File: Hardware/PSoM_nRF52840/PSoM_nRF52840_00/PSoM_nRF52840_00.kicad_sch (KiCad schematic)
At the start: 0 parts

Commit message: working on nrf52840
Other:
- sheet nRF52840 renamed 400-nRF52840
- sheet 100_Connectors ports: added CC1, CC2, RST, SWDCLK, SWDIO; removed EN, RX0, TX0
- sheet 200_1S_Charger ports: added 3V3_EXT, 3V3_nRF, CC1, CC2, VBUS_OUT; removed none
- sheet 400-nRF52840 ports: added D+, D-, GND, IO[0..42], SPI[0..7], SWDCLK, SWDIO, VBUS, VDD_nRF; removed none

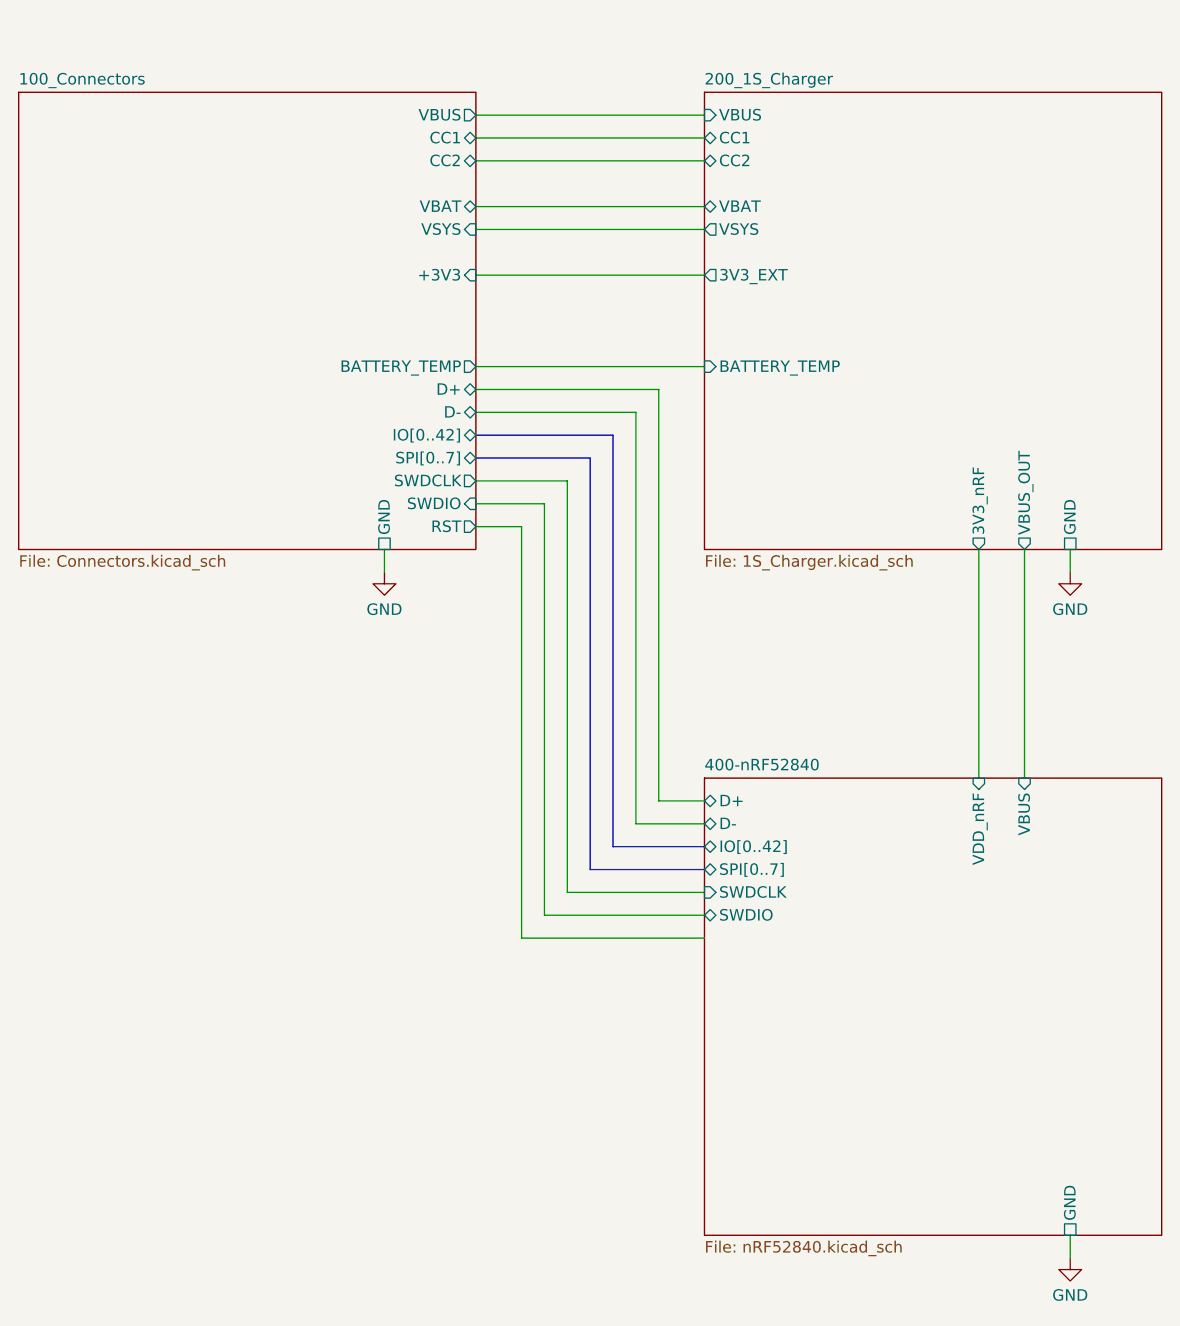
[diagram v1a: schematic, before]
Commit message: footprint assignement done
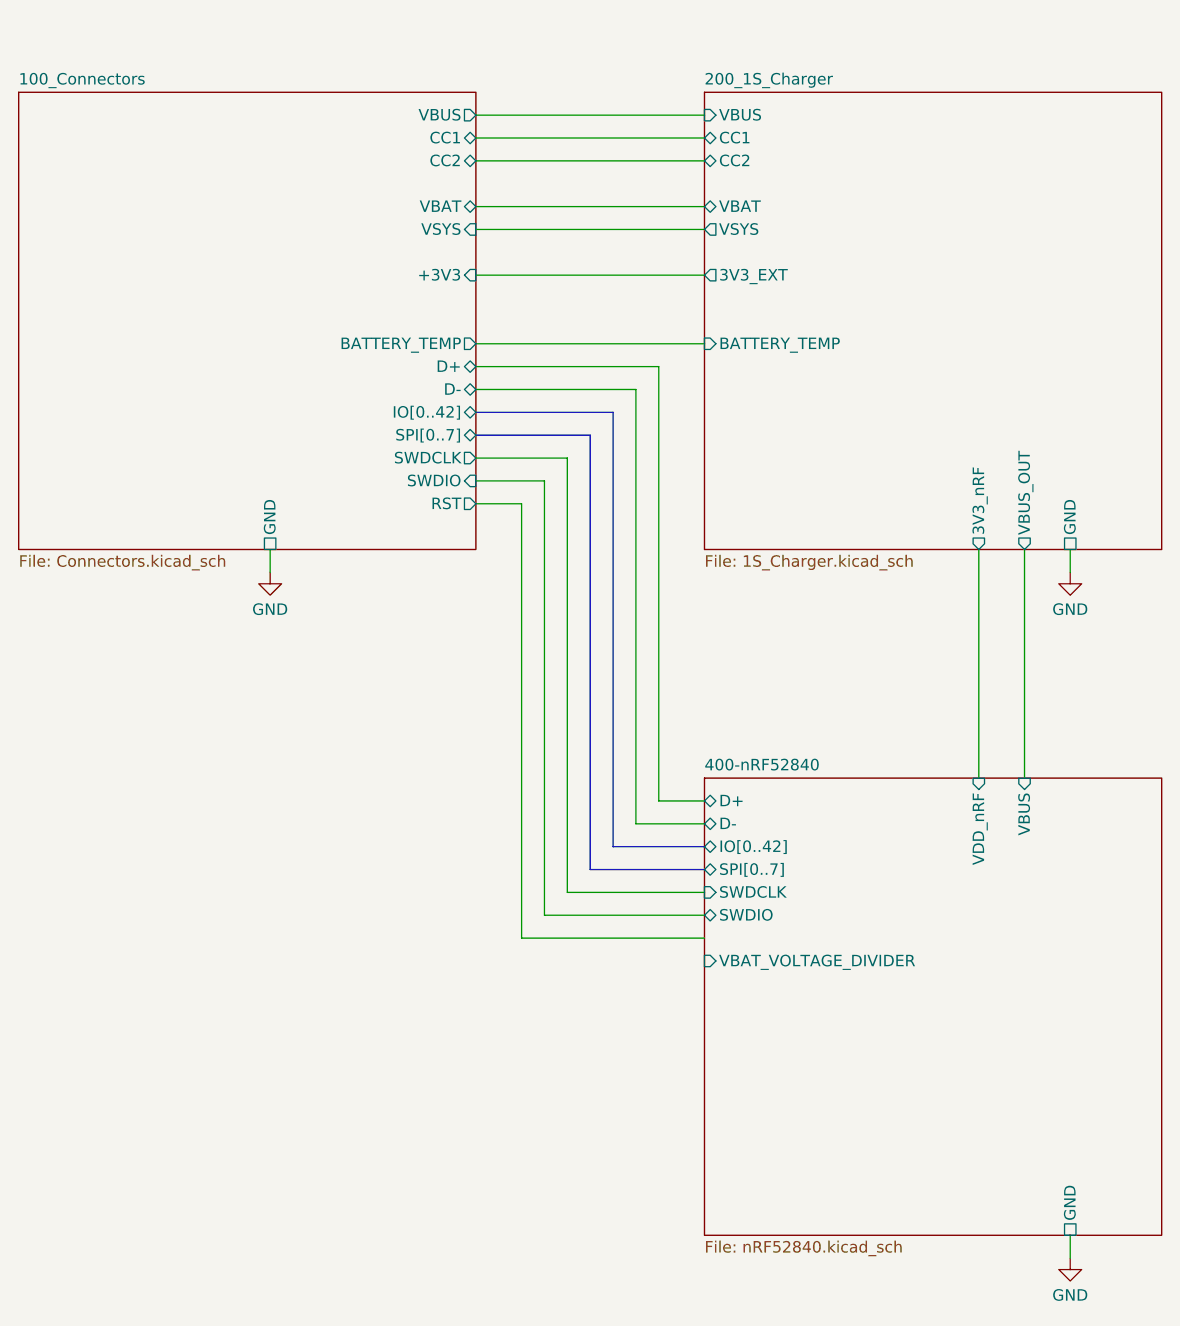
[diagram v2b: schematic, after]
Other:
- sheet 400-nRF52840 ports: added VBAT_VOLTAGE_DIVIDER; removed none
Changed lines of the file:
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@@
 	(wire
 		(pts
-			(xy 109.22 71.12) (xy 109.22 116.84)
+			(xy 109.22 68.58) (xy 109.22 116.84)
 		)
 		(stroke
@@
 	(wire
 		(pts
-			(xy 101.6 73.66) (xy 106.68 73.66)
-		)
-		(stroke
-			(width 0)
-			(type default)
-		)
-	)
-	(wire
-		(pts
-			(xy 91.44 76.2) (xy 91.44 78.74)
-		)
-		(stroke
-			(width 0)
-			(type default)
-		)
-	)
-	(wire
-		(pts
-			(xy 121.92 58.42) (xy 101.6 58.42)
-		)
-		(stroke
-			(width 0)
-			(type default)
-		)
-	)
-	(wire
-		(pts
-			(xy 106.68 73.66) (xy 106.68 119.38)
+			(xy 101.6 71.12) (xy 106.68 71.12)
+		)
+		(stroke
+			(width 0)
+			(type default)
+		)
+	)
+	(wire
+		(pts
+			(xy 78.74 76.2) (xy 78.74 78.74)
+		)
+		(stroke
+			(width 0)
+			(type default)
+		)
+	)
+	(wire
+		(pts
+			(xy 121.92 55.88) (xy 101.6 55.88)
+		)
+		(stroke
+			(width 0)
+			(type default)
+		)
+	)
+	(wire
+		(pts
+			(xy 106.68 71.12) (xy 106.68 119.38)
 		)
 		(stroke
@@
 	(wire
 		(pts
-			(xy 121.92 58.42) (xy 121.92 104.14)
+			(xy 121.92 55.88) (xy 121.92 104.14)
 		)
 		(stroke
@@
 	(wire
 		(pts
-			(xy 111.76 114.3) (xy 111.76 68.58)
+			(xy 111.76 114.3) (xy 111.76 66.04)
 		)
 		(stroke
@@
 	(bus
 		(pts
-			(xy 116.84 109.22) (xy 116.84 63.5)
+			(xy 116.84 109.22) (xy 116.84 60.96)
 		)
 		(stroke
@@
 	(wire
 		(pts
-			(xy 111.76 68.58) (xy 101.6 68.58)
+			(xy 111.76 66.04) (xy 101.6 66.04)
 		)
 		(stroke
@@
 	(bus
 		(pts
-			(xy 114.3 66.04) (xy 114.3 111.76)
+			(xy 114.3 63.5) (xy 114.3 111.76)
 		)
 		(stroke
@@
 	(wire
 		(pts
-			(xy 101.6 71.12) (xy 109.22 71.12)
-		)
-		(stroke
-			(width 0)
-			(type default)
-		)
-	)
-	(wire
-		(pts
-			(xy 119.38 60.96) (xy 119.38 106.68)
+			(xy 101.6 68.58) (xy 109.22 68.58)
+		)
+		(stroke
+			(width 0)
+			(type default)
+		)
+	)
+	(wire
+		(pts
+			(xy 119.38 58.42) (xy 119.38 106.68)
 		)
 		(stroke
@@
 	(bus
 		(pts
-			(xy 101.6 66.04) (xy 114.3 66.04)
-		)
-		(stroke
-			(width 0)
-			(type default)
-		)
-	)
-	(wire
-		(pts
-			(xy 101.6 60.96) (xy 119.38 60.96)
+			(xy 101.6 63.5) (xy 114.3 63.5)
+		)
+		(stroke
+			(width 0)
+			(type default)
+		)
+	)
+	(wire
+		(pts
+			(xy 101.6 58.42) (xy 119.38 58.42)
 		)
 		(stroke
@@
 	(bus
 		(pts
-			(xy 116.84 63.5) (xy 101.6 63.5)
-		)
-		(stroke
-			(width 0)
-			(type default)
-		)
-	)
-	(wire
-		(pts
-			(xy 101.6 55.88) (xy 127 55.88)
+			(xy 116.84 60.96) (xy 101.6 60.96)
+		)
+		(stroke
+			(width 0)
+			(type default)
+		)
+	)
+	(wire
+		(pts
+			(xy 101.6 53.34) (xy 127 53.34)
 		)
 		(stroke
@@
 	(symbol
 		(lib_id "power:GND")
-		(at 91.44 78.74 0)
+		(at 78.74 78.74 0)
 		(unit 1)
 		(exclude_from_sim no)
@@
 		(fields_autoplaced yes)
 		(property "Reference" "#PWR06"
-			(at 91.44 85.09 0)
+			(at 78.74 85.09 0)
 			(effects
 				(font
@@
 		)
 		(property "Value" "GND"
-			(at 91.44 82.8755 0)
+			(at 78.74 82.8755 0)
 			(effects
 				(font
@@
 		)
 		(property "Footprint" ""
-			(at 91.44 78.74 0)
+			(at 78.74 78.74 0)
 			(effects
 				(font
@@
 		)
 		(property "Datasheet" ""
-			(at 91.44 78.74 0)
+			(at 78.74 78.74 0)
 			(effects
 				(font
@@
 		)
 		(property "Description" ""
-			(at 91.44 78.74 0)
+			(at 78.74 78.74 0)
 			(effects
 				(font
@@
 		)
 		(pin "BATTERY_TEMP" input
-			(at 127 55.88 180)
+			(at 127 53.34 180)
 			(effects
 				(font
@@
 		)
 		(pin "D-" bidirectional
-			(at 101.6 60.96 0)
+			(at 101.6 58.42 0)
 			(effects
 				(font
@@
 		)
 		(pin "D+" bidirectional
-			(at 101.6 58.42 0)
+			(at 101.6 55.88 0)
 			(effects
 				(font
@@
 		)
 		(pin "GND" passive
-			(at 91.44 76.2 270)
+			(at 78.74 76.2 270)
 			(effects
 				(font
@@
 		)
 		(pin "IO[0..42]" bidirectional
-			(at 101.6 63.5 0)
+			(at 101.6 60.96 0)
 			(effects
 				(font
@@
 		)
 		(pin "SPI[0..7]" bidirectional
-			(at 101.6 66.04 0)
+			(at 101.6 63.5 0)
 			(effects
 				(font
@@
 		)
 		(pin "BATTERY_TEMP" output
-			(at 101.6 55.88 0)
+			(at 101.6 53.34 0)
 			(effects
 				(font
@@
 		)
 		(pin "SWDCLK" output
+			(at 101.6 66.04 0)
+			(effects
+				(font
+					(size 1.27 1.27)
+				)
+				(justify right)
+			)
+		)
+		(pin "SWDIO" input
 			(at 101.6 68.58 0)
-			(effects
-				(font
-					(size 1.27 1.27)
-				)
-				(justify right)
-			)
-		)
-		(pin "SWDIO" input
-			(at 101.6 71.12 0)
 			(effects
 				(font
@@
 		)
 		(pin "RST" output
-			(at 101.6 73.66 0)
+			(at 101.6 71.12 0)
 			(effects
 				(font
@@
 			)
 		)
+		(pin "VBAT_VOLTAGE_DIVIDER" input
+			(at 127 121.92 180)
+			(effects
+				(font
+					(size 1.27 1.27)
+				)
+				(justify left)
+			)
+		)

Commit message: working on schematic
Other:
- sheet 100_Connectors ports: added P[0..52]; removed IO[0..42]
- sheet 400-nRF52840 ports: added P[0..52], RESET; removed IO[0..42], VBAT_VOLTAGE_DIVIDER
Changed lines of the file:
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@@
 	(wire
 		(pts
-			(xy 78.74 76.2) (xy 78.74 78.74)
+			(xy 76.2 76.2) (xy 76.2 78.74)
 		)
 		(stroke
@@
 	(symbol
 		(lib_id "power:GND")
-		(at 78.74 78.74 0)
+		(at 76.2 78.74 0)
 		(unit 1)
 		(exclude_from_sim no)
@@
 		(fields_autoplaced yes)
 		(property "Reference" "#PWR06"
-			(at 78.74 85.09 0)
+			(at 76.2 85.09 0)
 			(effects
 				(font
@@
 		)
 		(property "Value" "GND"
-			(at 78.74 82.8755 0)
+			(at 76.2 82.8755 0)
 			(effects
 				(font
@@
 		)
 		(property "Footprint" ""
-			(at 78.74 78.74 0)
+			(at 76.2 78.74 0)
 			(effects
 				(font
@@
 		)
 		(property "Datasheet" ""
-			(at 78.74 78.74 0)
+			(at 76.2 78.74 0)
 			(effects
 				(font
@@
 		)
 		(property "Description" ""
-			(at 78.74 78.74 0)
+			(at 76.2 78.74 0)
 			(effects
 				(font
@@
 		)
 		(pin "GND" passive
-			(at 78.74 76.2 270)
-			(effects
-				(font
-					(size 1.27 1.27)
-				)
-				(justify left)
-			)
-		)
-		(pin "IO[0..42]" bidirectional
-			(at 101.6 60.96 0)
-			(effects
-				(font
-					(size 1.27 1.27)
-				)
-				(justify right)
+			(at 76.2 76.2 270)
+			(effects
+				(font
+					(size 1.27 1.27)
+				)
+				(justify left)
 			)
 		)
@@
 		(pin "RST" output
 			(at 101.6 71.12 0)
+			(effects
+				(font
+					(size 1.27 1.27)
+				)
+				(justify right)
+			)
+		)
+		(pin "P[0..52]" bidirectional
+			(at 101.6 60.96 0)
 			(effects
 				(font
@@
 			)
 		)
-		(pin "IO[0..42]" bidirectional
-			(at 127 109.22 180)
-			(effects
-				(font
-					(size 1.27 1.27)
-				)
-				(justify left)
-			)
-		)
 		(pin "VBUS" input
 			(at 162.56 101.6 90)
@@
 			)
 		)
-		(pin "VBAT_VOLTAGE_DIVIDER" input
-			(at 127 121.92 180)
-			(effects
-				(font
+		(pin "RESET" input
+			(at 127 119.38 180)
+			(effects
+				(font
+					(size 1.27 1.27)
+				)
+				(justify left)
+			)
+		)
+		(pin "P[0..52]" bidirectional
+			(at 127 109.22 180)
+			(effects
+				(font

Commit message: schematic should be done
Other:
- sheet 200_1S_Charger ports: added SCL, SDA; removed none
- sheet 400-nRF52840 ports: added SCL, SDA; removed none
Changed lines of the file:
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@@
+	(wire
+		(pts
+			(xy 167.64 101.6) (xy 167.64 76.2)
+		)
+		(stroke
+			(width 0)
+			(type default)
+		)
+	)
 	(wire
 		(pts
@@
 	(wire
 		(pts
-			(xy 162.56 76.2) (xy 162.56 101.6)
+			(xy 160.02 76.2) (xy 160.02 101.6)
 		)
 		(stroke
@@
 	(wire
 		(pts
+			(xy 165.1 76.2) (xy 165.1 101.6)
+		)
+		(stroke
+			(width 0)
+			(type default)
+		)
+	)
+	(wire
+		(pts
 			(xy 111.76 66.04) (xy 101.6 66.04)
 		)
@@
 	(wire
 		(pts
-			(xy 167.64 76.2) (xy 167.64 78.74)
+			(xy 175.26 76.2) (xy 175.26 78.74)
 		)
 		(stroke
@@
 	(symbol
 		(lib_id "power:GND")
-		(at 167.64 78.74 0)
+		(at 175.26 78.74 0)
 		(unit 1)
 		(exclude_from_sim no)
@@
 		(fields_autoplaced yes)
 		(property "Reference" "#PWR07"
-			(at 167.64 85.09 0)
+			(at 175.26 85.09 0)
 			(effects
 				(font
@@
 		)
 		(property "Value" "GND"
-			(at 167.64 82.8755 0)
+			(at 175.26 82.8755 0)
 			(effects
 				(font
@@
 		)
 		(property "Footprint" ""
-			(at 167.64 78.74 0)
+			(at 175.26 78.74 0)
 			(effects
 				(font
@@
 		)
 		(property "Datasheet" ""
-			(at 167.64 78.74 0)
+			(at 175.26 78.74 0)
 			(effects
 				(font
@@
 		)
 		(property "Description" ""
-			(at 167.64 78.74 0)
+			(at 175.26 78.74 0)
 			(effects
 				(font
@@
 		)
 		(pin "GND" passive
-			(at 167.64 76.2 270)
+			(at 175.26 76.2 270)
 			(effects
 				(font
@@
 		)
 		(pin "VBUS_OUT" output
-			(at 162.56 76.2 270)
+			(at 160.02 76.2 270)
 			(effects
 				(font
@@
 		(pin "CC1" bidirectional
 			(at 127 30.48 180)
+			(effects
+				(font
+					(size 1.27 1.27)
+				)
+				(justify left)
+			)
+		)
+		(pin "SCL" input
+			(at 167.64 76.2 270)
+			(effects
+				(font
+					(size 1.27 1.27)
+				)
+				(justify left)
+			)
+		)
+		(pin "SDA" bidirectional
+			(at 165.1 76.2 270)
 			(effects
 				(font
@@
 		)
 		(pin "VBUS" input
-			(at 162.56 101.6 90)
+			(at 160.02 101.6 90)
 			(effects
 				(font
@@
 			)
 		)
+		(pin "SDA" bidirectional
+			(at 165.1 101.6 90)
+			(effects
+				(font
+					(size 1.27 1.27)
+				)
+				(justify right)
+			)
+		)
+		(pin "SCL" output
+			(at 167.64 101.6 90)
+			(effects
+				(font
+					(size 1.27 1.27)
+				)
+				(justify right)
+			)
+		)

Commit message: moved the nrf away and re routed everything
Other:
- sheet 200_1S_Charger ports: added P[0..52]; removed SCL, SDA
- sheet 400-nRF52840 ports: added none; removed SCL, SDA
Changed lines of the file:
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@@
 		(company "PumaCorp")
 	)
+	(junction
+		(at 116.84 60.96)
+		(diameter 0)
+		(color 0 0 0 0)
+	)
 	(wire
 		(pts
@@
 		)
 	)
+	(bus
+		(pts
+			(xy 116.84 60.96) (xy 127 60.96)
+		)
+		(stroke
+			(width 0)
+			(type default)
+		)
+	)
 	(wire
 		(pts
@@
 	(wire
 		(pts
-			(xy 167.64 101.6) (xy 167.64 76.2)
-		)
-		(stroke
-			(width 0)
-			(type default)
-		)
-	)
-	(wire
-		(pts
 			(xy 121.92 55.88) (xy 101.6 55.88)
 		)
@@
 		(pts
 			(xy 106.68 119.38) (xy 127 119.38)
-		)
-		(stroke
-			(width 0)
-			(type default)
-		)
-	)
-	(wire
-		(pts
-			(xy 165.1 76.2) (xy 165.1 101.6)
 		)
 		(stroke
@@
 			)
 		)
-		(pin "SCL" input
-			(at 167.64 76.2 270)
-			(effects
-				(font
-					(size 1.27 1.27)
-				)
-				(justify left)
-			)
-		)
-		(pin "SDA" bidirectional
-			(at 165.1 76.2 270)
+		(pin "P[0..52]" bidirectional
+			(at 127 60.96 180)
 			(effects
 				(font
@@
 			)
 		)
-		(pin "SDA" bidirectional
-			(at 165.1 101.6 90)
-			(effects
-				(font
-					(size 1.27 1.27)
-				)
-				(justify right)
-			)
-		)
-		(pin "SCL" output
-			(at 167.64 101.6 90)
-			(effects
-				(font
-					(size 1.27 1.27)
-				)
-				(justify right)
-			)
-		)
